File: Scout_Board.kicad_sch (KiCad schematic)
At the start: 3 parts, among them U2 ESP32-S3-DEVKITC-1U-N8R2

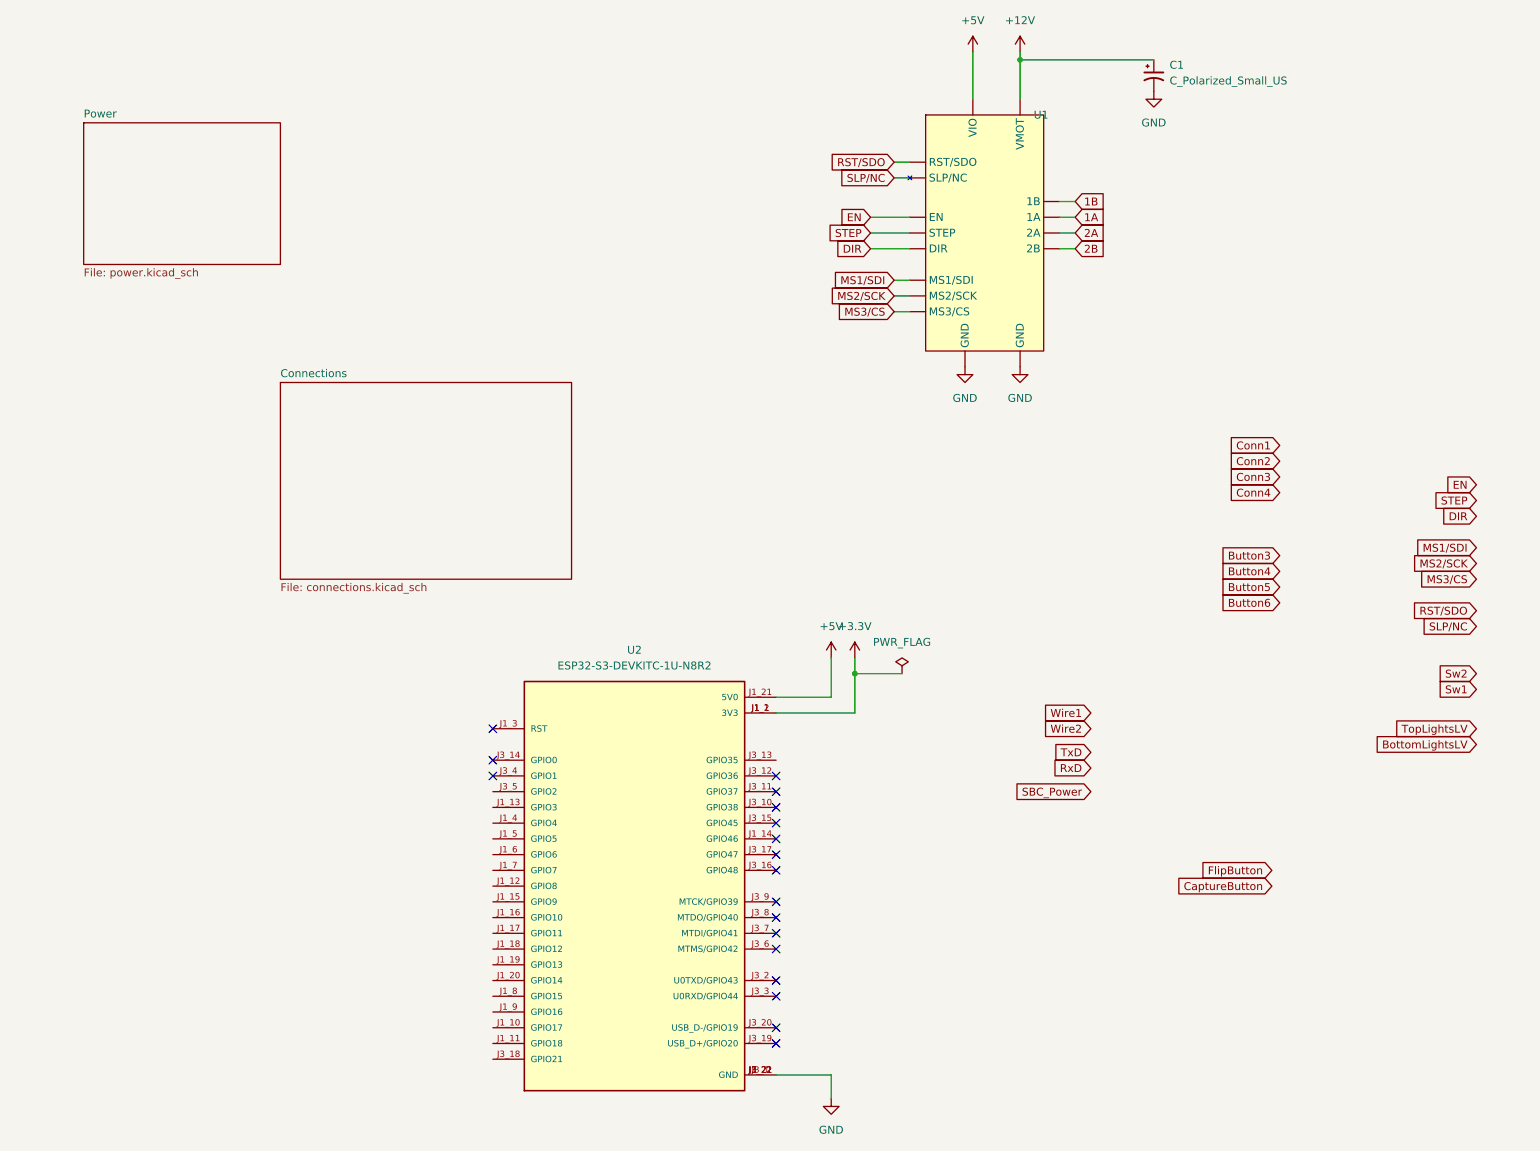
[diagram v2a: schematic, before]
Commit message: power board changes
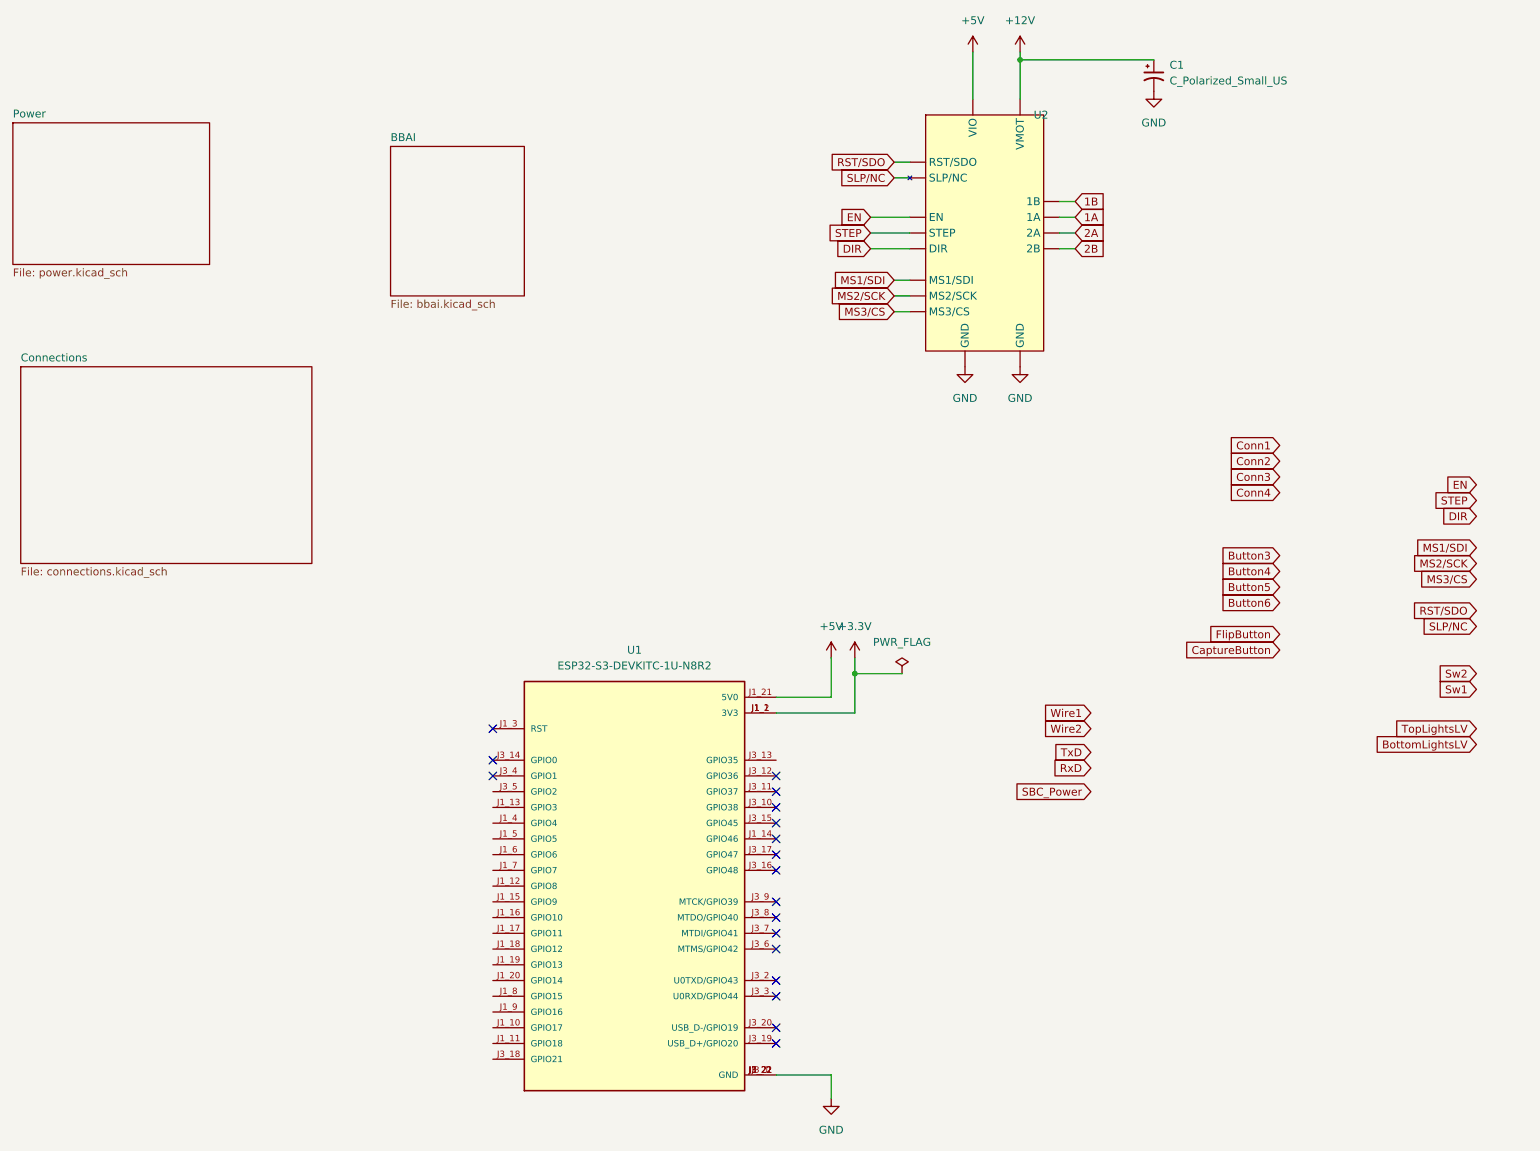
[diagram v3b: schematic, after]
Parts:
- renumbered U2 to U1, U1 to U2
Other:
- added sheet BBAI (bbai.kicad_sch)
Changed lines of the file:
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@@
 	(global_label "FlipButton"
 		(shape input)
-		(at 223.52 152.4 180)
-		(fields_autoplaced yes)
-		(effects
-			(font
-				(size 1.27 1.27)
-			)
-			(justify right)
-		)
-		(property "Intersheetrefs" "${INTERSHEET_REFS}"
-			(at 210.8588 152.4 0)
+		(at 224.79 114.3 180)
+		(fields_autoplaced yes)
+		(effects
+			(font
+				(size 1.27 1.27)
+			)
+			(justify right)
+		)
+		(property "Intersheetrefs" "${INTERSHEET_REFS}"
+			(at 212.1288 114.3 0)
 			(effects
 				(font
@@
 	(global_label "CaptureButton"
 		(shape input)
-		(at 223.52 154.94 180)
-		(fields_autoplaced yes)
-		(effects
-			(font
-				(size 1.27 1.27)
-			)
-			(justify right)
-		)
-		(property "Intersheetrefs" "${INTERSHEET_REFS}"
-			(at 207.0489 154.94 0)
+		(at 224.79 116.84 180)
+		(fields_autoplaced yes)
+		(effects
+			(font
+				(size 1.27 1.27)
+			)
+			(justify right)
+		)
+		(property "Intersheetrefs" "${INTERSHEET_REFS}"
+			(at 208.3189 116.84 0)
 			(effects
 				(font
@@
 		(dnp no)
 		(fields_autoplaced yes)
-		(property "Reference" "#PWR09"
+		(property "Reference" "#PWR06"
 			(at 182.88 24.13 0)
 			(effects
@@
 			(project ""
 				(path "/e58a9779-147f-4c0c-a745-6e9bc8ec0357"
-					(reference "#PWR09")
+					(reference "#PWR06")
 					(unit 1)
 				)
@@
 		(dnp no)
 		(fields_autoplaced yes)
-		(property "Reference" "U1"
+		(property "Reference" "U2"
 			(at 185.0741 30.48 0)
 			(effects
@@
 			(project ""
 				(path "/e58a9779-147f-4c0c-a745-6e9bc8ec0357"
-					(reference "U1")
+					(reference "U2")
 					(unit 1)
 				)
@@
 		(dnp no)
 		(fields_autoplaced yes)
-		(property "Reference" "#PWR059"
+		(property "Reference" "#PWR03"
 			(at 156.21 121.92 0)
 			(effects
@@
 			(project ""
 				(path "/e58a9779-147f-4c0c-a745-6e9bc8ec0357"
-					(reference "#PWR059")
+					(reference "#PWR03")
 					(unit 1)
 				)
@@
 		(dnp no)
 		(fields_autoplaced yes)
-		(property "Reference" "#PWR07"
+		(property "Reference" "#PWR02"
 			(at 152.4 195.58 0)
 			(effects
@@
 			(project "Scout_Board"
 				(path "/e58a9779-147f-4c0c-a745-6e9bc8ec0357"
-					(reference "#PWR07")
+					(reference "#PWR02")
 					(unit 1)
 				)
@@
 		(on_board yes)
 		(dnp no)
-		(property "Reference" "#PWR016"
+		(property "Reference" "#PWR07"
 			(at 182.88 77.47 0)
 			(effects
@@
 			(project "Scout_Board"
 				(path "/e58a9779-147f-4c0c-a745-6e9bc8ec0357"
-					(reference "#PWR016")
+					(reference "#PWR07")
 					(unit 1)
 				)
@@
 		(on_board yes)
 		(dnp no)
-		(property "Reference" "#PWR012"
+		(property "Reference" "#PWR04"
 			(at 173.99 77.47 0)
 			(effects
@@
 			(project "Scout_Board"
 				(path "/e58a9779-147f-4c0c-a745-6e9bc8ec0357"
-					(reference "#PWR012")
+					(reference "#PWR04")
 					(unit 1)
 				)
@@
 		(dnp no)
 		(fields_autoplaced yes)
-		(property "Reference" "U2"
+		(property "Reference" "U1"
 			(at 120.65 116.84 0)
 			(effects
@@
 			(project "Scout_Board"
 				(path "/e58a9779-147f-4c0c-a745-6e9bc8ec0357"
-					(reference "U2")
+					(reference "U1")
 					(unit 1)
 				)
@@
 		(dnp no)
 		(fields_autoplaced yes)
-		(property "Reference" "#PWR05"
+		(property "Reference" "#PWR01"
 			(at 152.4 121.92 0)
 			(effects
@@
 			(project "Scout_Board"
 				(path "/e58a9779-147f-4c0c-a745-6e9bc8ec0357"
-					(reference "#PWR05")
+					(reference "#PWR01")
 					(unit 1)
 				)
@@
 		(dnp no)
 		(fields_autoplaced yes)
-		(property "Reference" "#PWR01"
+		(property "Reference" "#PWR08"
 			(at 204.47 33.02 0)
 			(effects
@@
 			(project ""
 				(path "/e58a9779-147f-4c0c-a745-6e9bc8ec0357"
-					(reference "#PWR01")
+					(reference "#PWR08")
 					(unit 1)
 				)
@@
 		(dnp no)
 		(fields_autoplaced yes)
-		(property "Reference" "#PWR02"
+		(property "Reference" "#PWR05"
 			(at 175.26 24.13 0)
 			(effects
@@
 			(project "Scout_Board"
 				(path "/e58a9779-147f-4c0c-a745-6e9bc8ec0357"
-					(reference "#PWR02")
+					(reference "#PWR05")
 					(unit 1)
 				)
@@
 	)
 	(sheet
-		(at 63.5 73.66)
+		(at 21.59 71.12)
 		(size 46.99 31.75)
 		(fields_autoplaced yes)
@@
 		)
 		(property "Sheetname" "Connections"
-			(at 63.5 72.9484 0)
+			(at 21.59 70.4084 0)
 			(effects
 				(font
@@
 		)
 		(property "Sheetfile" "connections.kicad_sch"
-			(at 63.5 105.9946 0)
+			(at 21.59 103.4546 0)
 			(effects
 				(font
@@
 	)
 	(sheet
-		(at 31.75 31.75)
+		(at 20.32 31.75)
 		(size 31.75 22.86)
 		(fields_autoplaced yes)
@@
 		)
 		(property "Sheetname" "Power"
-			(at 31.75 31.0384 0)
+			(at 20.32 31.0384 0)
 			(effects
 				(font
@@
 		)
 		(property "Sheetfile" "power.kicad_sch"
-			(at 31.75 55.1946 0)
+			(at 20.32 55.1946 0)
 			(effects
 				(font
@@
 				)
 			)
+		)
+	)
+	(sheet
+		(at 81.28 35.56)
+		(size 21.59 24.13)
+		(fields_autoplaced yes)
+		(stroke
+			(width 0.1524)
+			(type solid)
+		)
+		(fill
+			(color 0 0 0 0.0000)
+		)
+		(property "Sheetname" "BBAI"
+			(at 81.28 34.8484 0)
+			(effects
+				(font
+					(size 1.27 1.27)
+				)
+				(justify left bottom)
+			)
+		)
+		(property "Sheetfile" "bbai.kicad_sch"
+			(at 81.28 60.2746 0)
+			(effects
+				(font
+					(size 1.27 1.27)
+				)
+				(justify left top)
+			)
+		)
+		(property "Field2" ""
+			(at 81.28 35.56 0)
+			(effects
+				(font
+					(size 1.27 1.27)
+				)
+				(hide yes)
+			)
+		)
+		(instances
+			(project "Scout_Board"
+				(path "/e58a9779-147f-4c0c-a745-6e9bc8ec0357"
+					(page "4")
+				)
+			)

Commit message: New board test
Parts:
- C1: value C_Polarized_Small_US -> 100uF/16V; footprint (none) -> Capacitor_SMD:CP_Elec_6.3x5.9
- U1: footprint Downloaded_footprints:XCVR_ESP32-S3-DEVKITC-1U-N8R2 -> ESP32-S3-DEVKITC-1-N8R2:XCVR_ESP32-S3-DEVKITC-1-N8R2
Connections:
- net +12V: now also U2.16 (VMOT); no longer U2. (SLP/NC)
- net +5V: now also U2.10 (VIO); no longer U2. (SLP/NC)
- net 1A: now also U2.12 (1A); no longer U2. (SLP/NC)
- net 1B: now also U2.11 (1B); no longer U2. (SLP/NC)
- net 2A: now also U2.13 (2A); no longer U2. (SLP/NC)
- net 2B: now also U2.14 (2B); no longer U2. (SLP/NC)
- net BottomLightsLV: now also U1.J1_19 (GPIO13)
- net CaptureButton: now also U1.J3_11 (GPIO37)
- net Conn1: now also U1.J3_16 (GPIO48)
- net Conn2: now also U1.J3_17 (GPIO47)
- net Conn3: now also U1.J1_14 (GPIO46)
- net Conn4: now also U1.J3_15 (GPIO45)
- net DIR: now also U1.J1_4 (GPIO4), U2.8 (DIR); no longer U2. (SLP/NC)
- net EN: now also U1.J3_5 (GPIO2), U2.1 (EN); no longer U2. (SLP/NC)
- net FlipButton: now also U1.J3_10 (GPIO38)
- net GND: now also U2.15 (GND), U2.9 (GND); no longer U2. (SLP/NC)
- net MS1/SDI: now also U1.J1_5 (GPIO5), U2.2 (MS1/SDI); no longer U2. (SLP/NC)
- net MS2/SCK: now also U1.J1_6 (GPIO6), U2.3 (MS2/SCK); no longer U2. (SLP/NC)
- net MS3/CS: now also U1.J1_7 (GPIO7), U2.4 (MS3/CS); no longer U2. (SLP/NC)
- net RST/SDO: now also U1.J1_12 (GPIO8), U2.5 (RST/SDO); no longer U2. (SLP/NC)
- net RxD: now also U1.J1_10 (GPIO17)
- net SBC_Power: now also U1.J1_11 (GPIO18)
- net SLP/NC: now also U1.J1_15 (GPIO9), U2.6 (SLP/NC); no longer U2. (SLP/NC)
- net STEP: now also U1.J1_13 (GPIO3), U2.7 (STEP); no longer U2. (SLP/NC)
- net Sw1: now also U1.J1_17 (GPIO11)
- net Sw2: now also U1.J1_16 (GPIO10)
- net TopLightsLV: now also U1.J1_18 (GPIO12)
- net TxD: now also U1.J1_9 (GPIO16)
- net Wire1: now also U1.J1_20 (GPIO14)
- net Wire2: now also U1.J1_8 (GPIO15)
- net Sys_reset: now reaches U1.J3_18 (GPIO21)
- no-connect marks 18 -> 3
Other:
- moved on the sheet: U1

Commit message: Layout changes
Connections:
- net BottomLightsLV: no longer U1.J1_19 (GPIO13)
- net CaptureButton: no longer U1.J3_11 (GPIO37)
- net Conn1: no longer U1.J3_16 (GPIO48)
- net Conn2: no longer U1.J3_17 (GPIO47)
- net Conn3: no longer U1.J1_14 (GPIO46)
- net Conn4: no longer U1.J3_15 (GPIO45)
- net DIR: no longer U1.J1_4 (GPIO4)
- net EN: no longer U1.J3_5 (GPIO2)
- net FlipButton: no longer U1.J3_10 (GPIO38)
- net MS1/SDI: no longer U1.J1_5 (GPIO5)
- net MS2/SCK: no longer U1.J1_6 (GPIO6)
- net MS3/CS: no longer U1.J1_7 (GPIO7)
- net RST/SDO: no longer U1.J1_12 (GPIO8)
- net RxD: no longer U1.J1_10 (GPIO17)
- net SBC_Power: no longer U1.J1_11 (GPIO18)
- net SLP/NC: no longer U1.J1_15 (GPIO9)
- net STEP: no longer U1.J1_13 (GPIO3)
- net Sw1: no longer U1.J1_17 (GPIO11)
- net Sw2: no longer U1.J1_16 (GPIO10)
- net Sys_reset: no longer U1.J3_18 (GPIO21)
- net TopLightsLV: no longer U1.J1_18 (GPIO12)
- net TxD: no longer U1.J1_9 (GPIO16)
- net Wire1: no longer U1.J1_20 (GPIO14)
- net Wire2: no longer U1.J1_8 (GPIO15)
